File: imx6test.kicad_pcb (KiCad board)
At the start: 2 copper layers, 12 parts

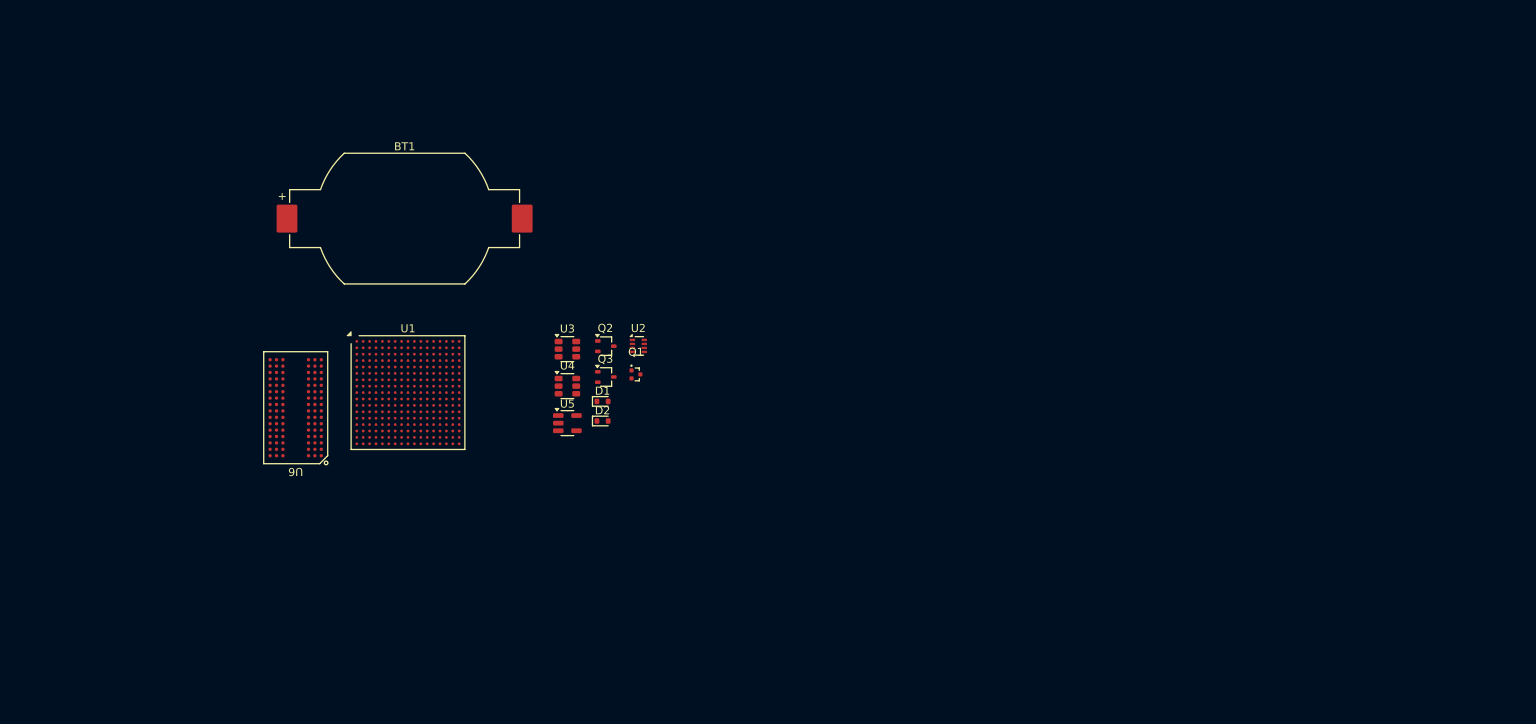
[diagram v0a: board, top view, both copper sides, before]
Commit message: Add in LCSC part numbers for major parts, assign packages
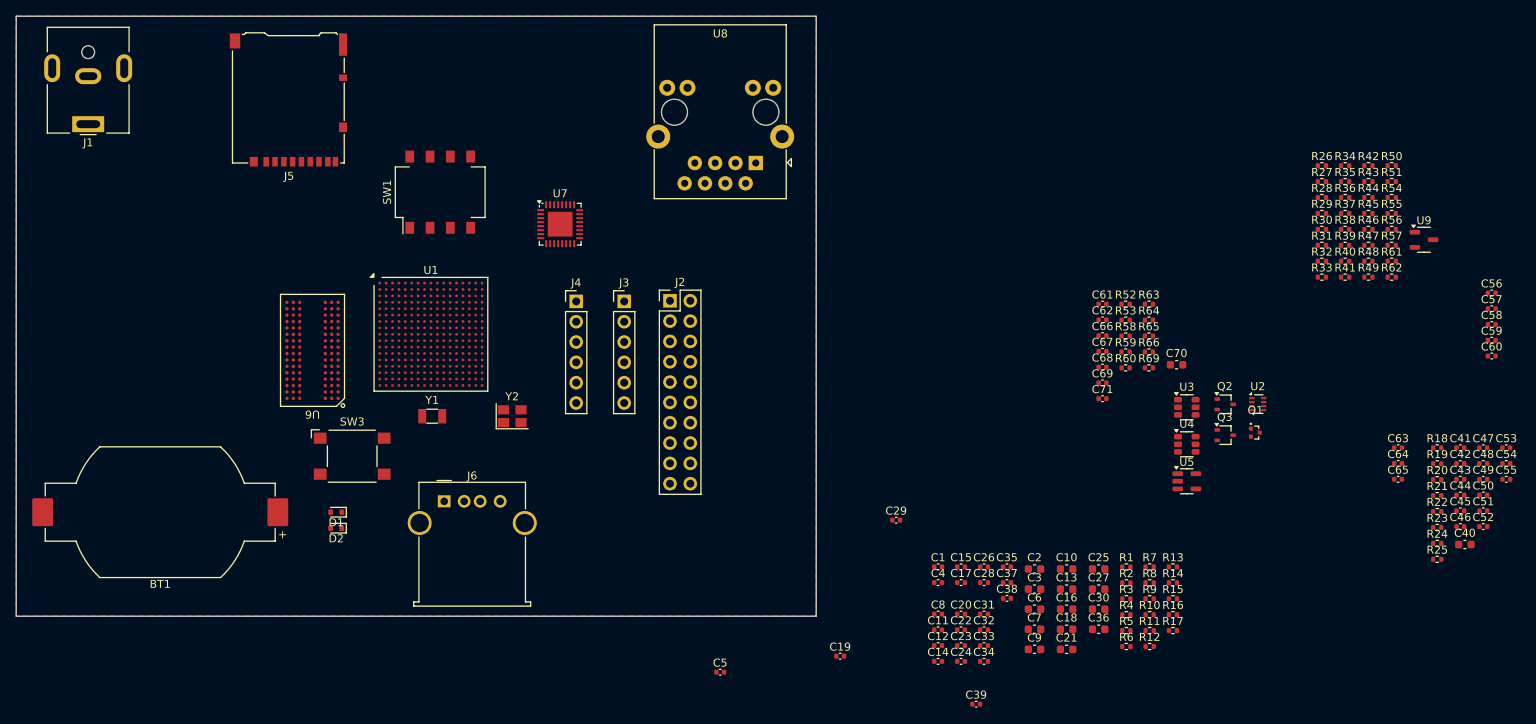
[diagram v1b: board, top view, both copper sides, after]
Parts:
- added C1: 0.1uF, Capacitor_SMD:C_0402_1005Metric, F.Cu at (220.2, 118.8)
- added C10: 10uF, Capacitor_SMD:C_0603_1608Metric, F.Cu at (236.3, 119.1)
- added C11: 0.1uF, Capacitor_SMD:C_0402_1005Metric, F.Cu at (220.2, 126.7)
- added C12: 22pF, Capacitor_SMD:C_0402_1005Metric, F.Cu at (220.2, 128.7)
- added C13: 22uF, Capacitor_SMD:C_0603_1608Metric, F.Cu at (236.3, 121.6)
- added C14: 0.1uF, Capacitor_SMD:C_0402_1005Metric, F.Cu at (220.2, 130.7)
- added C15: 22pF, Capacitor_SMD:C_0402_1005Metric, F.Cu at (223.1, 118.8)
- added C16: 22uF, Capacitor_SMD:C_0603_1608Metric, F.Cu at (236.3, 124.1)
- added C17: 0.1uF, Capacitor_SMD:C_0402_1005Metric, F.Cu at (223.1, 120.8)
- added C18: 22uF, Capacitor_SMD:C_0603_1608Metric, F.Cu at (236.3, 126.6)
- added C19: 0.22uF, Capacitor_SMD:C_0402_1005Metric, F.Cu at (208.0, 130.0)
- added C2: 10uF, Capacitor_SMD:C_0603_1608Metric, F.Cu at (232.3, 119.1)
- added C20: 0.22uF, Capacitor_SMD:C_0402_1005Metric, F.Cu at (223.1, 124.7)
- added C21: 22uF, Capacitor_SMD:C_0603_1608Metric, F.Cu at (236.3, 129.1)
- added C22: 0.22uF, Capacitor_SMD:C_0402_1005Metric, F.Cu at (223.1, 126.7)
- added C23: 0.22uF, Capacitor_SMD:C_0402_1005Metric, F.Cu at (223.1, 128.7)
- added C24: 0.22uF, Capacitor_SMD:C_0402_1005Metric, F.Cu at (223.1, 130.7)
- added C25: 10uF, Capacitor_SMD:C_0603_1608Metric, F.Cu at (240.3, 119.1)
- added C26: 0.22uF, Capacitor_SMD:C_0402_1005Metric, F.Cu at (226.0, 118.8)
- added C27: 10uF, Capacitor_SMD:C_0603_1608Metric, F.Cu at (240.3, 121.6)
- added C28: 0.22uF, Capacitor_SMD:C_0402_1005Metric, F.Cu at (226.0, 120.8)
- added C29: 0.22uF, Capacitor_SMD:C_0402_1005Metric, F.Cu at (215.0, 113.0)
- added C3: 10uF, Capacitor_SMD:C_0603_1608Metric, F.Cu at (232.3, 121.6)
- added C30: 22uF, Capacitor_SMD:C_0603_1608Metric, F.Cu at (240.3, 124.1)
- added C31: 4.7uF, Capacitor_SMD:C_0402_1005Metric, F.Cu at (226.0, 124.7)
- added C32: 0.22uF, Capacitor_SMD:C_0402_1005Metric, F.Cu at (226.0, 126.7)
- added C33: 0.22uF, Capacitor_SMD:C_0402_1005Metric, F.Cu at (226.0, 128.7)
- added C34: 4.7uF, Capacitor_SMD:C_0402_1005Metric, F.Cu at (226.0, 130.7)
- added C35: 0.22uF, Capacitor_SMD:C_0402_1005Metric, F.Cu at (228.8, 118.8)
- added C36: 10uF, Capacitor_SMD:C_0603_1608Metric, F.Cu at (240.3, 126.6)
- added C37: 0.1uF, Capacitor_SMD:C_0402_1005Metric, F.Cu at (228.8, 120.8)
- added C38: 4.7uF, Capacitor_SMD:C_0402_1005Metric, F.Cu at (228.8, 122.8)
- added C39: 0.1uF, Capacitor_SMD:C_0402_1005Metric, F.Cu at (225.0, 136.0)
- added C4: 0.22uF, Capacitor_SMD:C_0402_1005Metric, F.Cu at (220.2, 120.8)
- added C40: 10uF, Capacitor_SMD:C_0603_1608Metric, F.Cu at (286.1, 116.0)
- added C41: 0.22uF, Capacitor_SMD:C_0402_1005Metric, F.Cu at (285.5, 104.0)
- added C42: 0.22uF, Capacitor_SMD:C_0402_1005Metric, F.Cu at (285.5, 105.9)
- added C43: 0.22uF, Capacitor_SMD:C_0402_1005Metric, F.Cu at (285.5, 107.9)
- added C44: 0.22uF, Capacitor_SMD:C_0402_1005Metric, F.Cu at (285.5, 109.9)
- added C45: 0.22uF, Capacitor_SMD:C_0402_1005Metric, F.Cu at (285.5, 111.8)
- added C46: 0.22uF, Capacitor_SMD:C_0402_1005Metric, F.Cu at (285.5, 113.8)
- added C47: 0.22uF, Capacitor_SMD:C_0402_1005Metric, F.Cu at (288.4, 104.0)
- added C48: 0.22uF, Capacitor_SMD:C_0402_1005Metric, F.Cu at (288.4, 105.9)
- added C49: 0.22uF, Capacitor_SMD:C_0402_1005Metric, F.Cu at (288.4, 107.9)
- added C5: 2.2nF, Capacitor_SMD:C_0402_1005Metric, F.Cu at (193.0, 132.0)
- added C50: 0.22uF, Capacitor_SMD:C_0402_1005Metric, F.Cu at (288.4, 109.9)
- added C51: 4.7uF, Capacitor_SMD:C_0402_1005Metric, F.Cu at (288.4, 111.8)
- added C52: 0.1uF, Capacitor_SMD:C_0402_1005Metric, F.Cu at (288.4, 113.8)
- added C53: 0.1uF, Capacitor_SMD:C_0402_1005Metric, F.Cu at (291.3, 104.0)
- added C54: 2.2pF, Capacitor_SMD:C_0402_1005Metric, F.Cu at (291.3, 105.9)
- added C55: 2.2pF, Capacitor_SMD:C_0402_1005Metric, F.Cu at (291.3, 107.9)
- added C56: 18pF, Capacitor_SMD:C_0402_1005Metric, F.Cu at (289.4, 84.6)
- added C57: 18pF, Capacitor_SMD:C_0402_1005Metric, F.Cu at (289.4, 86.6)
- added C58: 18pF, Capacitor_SMD:C_0402_1005Metric, F.Cu at (289.4, 88.5)
- added C59: 18pF, Capacitor_SMD:C_0402_1005Metric, F.Cu at (289.4, 90.5)
- added C6: 10uF, Capacitor_SMD:C_0603_1608Metric, F.Cu at (232.3, 124.1)
- added C60: 0.22uF, Capacitor_SMD:C_0402_1005Metric, F.Cu at (289.4, 92.5)
- added C61: 0.22uF, Capacitor_SMD:C_0402_1005Metric, F.Cu at (240.8, 86.0)
- added C62: 0.22uF, Capacitor_SMD:C_0402_1005Metric, F.Cu at (240.8, 88.0)
- added C63: 0.22uF, Capacitor_SMD:C_0402_1005Metric, F.Cu at (277.7, 104.0)
- added C64: 0.22uF, Capacitor_SMD:C_0402_1005Metric, F.Cu at (277.7, 105.9)
- added C65: 0.22uF, Capacitor_SMD:C_0402_1005Metric, F.Cu at (277.7, 107.9)
- added C66: 0.1uF, Capacitor_SMD:C_0402_1005Metric, F.Cu at (240.8, 89.9)
- added C67: 2.2uF, Capacitor_SMD:C_0402_1005Metric, F.Cu at (240.8, 91.9)
- added C68: 0.1uF, Capacitor_SMD:C_0402_1005Metric, F.Cu at (240.8, 93.9)
- added C69: 0.1uF, Capacitor_SMD:C_0402_1005Metric, F.Cu at (240.8, 95.8)
- added C7: 10uF, Capacitor_SMD:C_0603_1608Metric, F.Cu at (232.3, 126.6)
- added C70: 10uF, Capacitor_SMD:C_0603_1608Metric, F.Cu at (250.1, 93.6)
- added C71: 0.1uF, Capacitor_SMD:C_0402_1005Metric, F.Cu at (240.8, 97.8)
- added C8: 0.1uF, Capacitor_SMD:C_0402_1005Metric, F.Cu at (220.2, 124.7)
- added C9: 10uF, Capacitor_SMD:C_0603_1608Metric, F.Cu at (232.3, 129.1)
- added J1: Barrel_Jack_MountingPin, Connector_BarrelJack:BarrelJack_CUI_PJ-063AH_Horizontal, F.Cu at (114.0, 63.5)
- added J2: Conn_ARM_JTAG_SWD_20, Connector_PinHeader_2.54mm:PinHeader_2x10_P2.54mm_Vertical, F.Cu at (186.7, 85.6)
- added J3: Conn_01x06_Pin, Connector_PinHeader_2.54mm:PinHeader_1x06_P2.54mm_Vertical, F.Cu at (181.0, 85.7)
- added J4: Conn_01x06_Pin, Connector_PinHeader_2.54mm:PinHeader_1x06_P2.54mm_Vertical, F.Cu at (175.0, 85.7)
- added J5: Micro_SD_Card_Det2, Connector_Card:microSD_HC_Hirose_DM3AT-SF-PEJM5, F.Cu at (139.0, 60.5)
- added J6: USB_A, Connector_USB:USB_A_Molex_67643_Horizontal, F.Cu at (158.5, 110.6)
- added R1: 200k 1%, Resistor_SMD:R_0402_1005Metric, F.Cu at (243.8, 118.8)
- added R10: 90.9k, Resistor_SMD:R_0402_1005Metric, F.Cu at (246.7, 124.8)
- added R11: 1k, Resistor_SMD:R_0402_1005Metric, F.Cu at (246.7, 126.8)
- added R12: 953k, Resistor_SMD:R_0402_1005Metric, F.Cu at (246.7, 128.8)
- added R13: 100k, Resistor_SMD:R_0402_1005Metric, F.Cu at (249.6, 118.8)
- added R14: 464k, Resistor_SMD:R_0402_1005Metric, F.Cu at (249.6, 120.8)
- added R15: 200k 1%, Resistor_SMD:R_0402_1005Metric, F.Cu at (249.6, 122.8)
- added R16: 243k, Resistor_SMD:R_0402_1005Metric, F.Cu at (249.6, 124.8)
- added R17: 100k, Resistor_SMD:R_0402_1005Metric, F.Cu at (249.6, 126.8)
- added R18: 10k, Resistor_SMD:R_0402_1005Metric, F.Cu at (282.6, 104.0)
- added R19: 240 1%, Resistor_SMD:R_0402_1005Metric, F.Cu at (282.6, 106.0)
- added R2: 44.2k 1%, Resistor_SMD:R_0402_1005Metric, F.Cu at (243.8, 120.8)
- added R20: 10k, Resistor_SMD:R_0402_1005Metric, F.Cu at (282.6, 107.9)
- added R21: 10k, Resistor_SMD:R_0402_1005Metric, F.Cu at (282.6, 109.9)
- added R22: 240 1%, Resistor_SMD:R_0402_1005Metric, F.Cu at (282.6, 111.9)
- added R23: 1.5k 1%, Resistor_SMD:R_0402_1005Metric, F.Cu at (282.6, 113.9)
- added R24: 1.5k 1%, Resistor_SMD:R_0402_1005Metric, F.Cu at (282.6, 115.9)
- added R25: 470, Resistor_SMD:R_0402_1005Metric, F.Cu at (282.6, 117.9)
- added R26: 10k, Resistor_SMD:R_0402_1005Metric, F.Cu at (268.2, 68.7)
- added R27: 10k, Resistor_SMD:R_0402_1005Metric, F.Cu at (268.2, 70.7)
- added R28: 10k, Resistor_SMD:R_0402_1005Metric, F.Cu at (268.2, 72.7)
- added R29: 10k, Resistor_SMD:R_0402_1005Metric, F.Cu at (268.2, 74.7)
- added R3: 10k, Resistor_SMD:R_0402_1005Metric, F.Cu at (243.8, 122.8)
- added R30: 10k, Resistor_SMD:R_0402_1005Metric, F.Cu at (268.2, 76.7)
- added R31: 10k, Resistor_SMD:R_0402_1005Metric, F.Cu at (268.2, 78.6)
- added R32: 10k, Resistor_SMD:R_0402_1005Metric, F.Cu at (268.2, 80.6)
- added R33: 10k, Resistor_SMD:R_0402_1005Metric, F.Cu at (268.2, 82.6)
- added R34: 10k, Resistor_SMD:R_0402_1005Metric, F.Cu at (271.1, 68.7)
- added R35: 10k, Resistor_SMD:R_0402_1005Metric, F.Cu at (271.1, 70.7)
- added R36: 10k, Resistor_SMD:R_0402_1005Metric, F.Cu at (271.1, 72.7)
- added R37: 10k, Resistor_SMD:R_0402_1005Metric, F.Cu at (271.1, 74.7)
- added R38: 10k, Resistor_SMD:R_0402_1005Metric, F.Cu at (271.1, 76.7)
- added R39: 10k, Resistor_SMD:R_0402_1005Metric, F.Cu at (271.1, 78.6)
- added R4: 10k, Resistor_SMD:R_0402_1005Metric, F.Cu at (243.8, 124.8)
- added R40: 10k, Resistor_SMD:R_0402_1005Metric, F.Cu at (271.1, 80.6)
- added R41: 10k, Resistor_SMD:R_0402_1005Metric, F.Cu at (271.1, 82.6)
- added R42: 10k, Resistor_SMD:R_0402_1005Metric, F.Cu at (274.0, 68.7)
- added R43: 10k, Resistor_SMD:R_0402_1005Metric, F.Cu at (274.0, 70.7)
- added R44: 10k, Resistor_SMD:R_0402_1005Metric, F.Cu at (274.0, 72.7)
- added R45: 10k, Resistor_SMD:R_0402_1005Metric, F.Cu at (274.0, 74.7)
- added R46: 10k, Resistor_SMD:R_0402_1005Metric, F.Cu at (274.0, 76.7)
- added R47: 10k, Resistor_SMD:R_0402_1005Metric, F.Cu at (274.0, 78.6)
- added R48: 10k, Resistor_SMD:R_0402_1005Metric, F.Cu at (274.0, 80.6)
- added R49: 10k, Resistor_SMD:R_0402_1005Metric, F.Cu at (274.0, 82.6)
- added R5: 10k, Resistor_SMD:R_0402_1005Metric, F.Cu at (243.8, 126.8)
- added R50: 1k, Resistor_SMD:R_0402_1005Metric, F.Cu at (276.9, 68.7)
- added R51: 10k, Resistor_SMD:R_0402_1005Metric, F.Cu at (276.9, 70.7)
- added R52: 6.49k, Resistor_SMD:R_0402_1005Metric, F.Cu at (243.7, 86.0)
- added R53: 220, Resistor_SMD:R_0402_1005Metric, F.Cu at (243.7, 88.0)
- added R54: 10k, Resistor_SMD:R_0402_1005Metric, F.Cu at (276.9, 72.7)
- added R55: 1k, Resistor_SMD:R_0402_1005Metric, F.Cu at (276.9, 74.7)
- added R56: 1k, Resistor_SMD:R_0402_1005Metric, F.Cu at (276.9, 76.7)
- added R57: 1k, Resistor_SMD:R_0402_1005Metric, F.Cu at (276.9, 78.6)
- added R58: 220, Resistor_SMD:R_0402_1005Metric, F.Cu at (243.7, 90.0)
- added R59: 1k, Resistor_SMD:R_0402_1005Metric, F.Cu at (243.7, 92.0)
- added R6: 127k, Resistor_SMD:R_0402_1005Metric, F.Cu at (243.8, 128.8)
- added R60: 1k, Resistor_SMD:R_0402_1005Metric, F.Cu at (243.7, 94.0)
- added R61: 10k, Resistor_SMD:R_0402_1005Metric, F.Cu at (276.9, 80.6)
- added R62: 1k, Resistor_SMD:R_0402_1005Metric, F.Cu at (276.9, 82.6)
- added R63: 1k, Resistor_SMD:R_0402_1005Metric, F.Cu at (246.6, 86.0)
- added R64: 1k, Resistor_SMD:R_0402_1005Metric, F.Cu at (246.6, 88.0)
- added R65: 1k, Resistor_SMD:R_0402_1005Metric, F.Cu at (246.6, 90.0)
- added R66: 4.7k, Resistor_SMD:R_0402_1005Metric, F.Cu at (246.6, 92.0)
- added R69: 4.7k, Resistor_SMD:R_0402_1005Metric, F.Cu at (246.6, 94.0)
- added R7: 100k 1%, Resistor_SMD:R_0402_1005Metric, F.Cu at (246.7, 118.8)
- added R8: 133k, Resistor_SMD:R_0402_1005Metric, F.Cu at (246.7, 120.8)
- added R9: 100k 1%, Resistor_SMD:R_0402_1005Metric, F.Cu at (246.7, 122.8)
- added SW1: SW_DIP_x04, Button_Switch_SMD:SW_DIP_SPSTx04_Slide_Omron_A6S-410x_W8.9mm_P2.54mm, F.Cu at (158.0, 72.0)
- added SW3: SW_SPST, Button_Switch_SMD:SW_SPST_Omron_B3FS-100xP, F.Cu at (147.0, 105.0)
- added U7: ~, Package_DFN_QFN:QFN-32-1EP_5x5mm_P0.5mm_EP3.1x3.1mm, F.Cu at (173.0, 76.0)
- added U8: ~, imx6test:HR9011105A, F.Cu at (193.0, 62.0)
- added U9: ~, Package_TO_SOT_SMD:SOT-23-3, F.Cu at (281.0, 77.9)
- added Y1: 32.768k, Crystal:Crystal_SMD_3215-2Pin_3.2x1.5mm, F.Cu at (157.0, 100.0)
- added Y2: 24MHz, Crystal:Crystal_SMD_SeikoEpson_TSX3225-4Pin_3.2x2.5mm, F.Cu at (167.0, 100.0)
- moved Q1 77.8 mm to (259.9, 102.0)
- moved Q2 77.8 mm to (256.1, 98.5)
- moved Q3 77.8 mm to (256.1, 102.4)
- moved U2 77.8 mm to (260.2, 98.5)
- moved U3 77.8 mm to (251.3, 98.9)
- moved U4 77.8 mm to (251.3, 103.5)
- moved U5 77.8 mm to (251.3, 108.1)
- moved BT1 47.8 mm to (123.0, 112.0), turned to 180 degrees
- moved D1 36.1 mm to (145.0, 112.0), turned to 180 degrees
- moved D2 35.9 mm to (145.0, 114.0), turned to 180 degrees
- moved U1 7.83 mm to (156.8, 89.8)
- moved U6 7.47 mm to (142.0, 91.8)
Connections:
- U1 pad A10: unconnected-(U1G-LCD_DATA06-PadA10) -> /Boot and Control/BOOT_CFG1(6)
- U1 pad A11: unconnected-(U1G-LCD_DATA09-PadA11) -> /Boot and Control/BOOT_CFG2(1)
- U1 pad A12: unconnected-(U1G-LCD_DATA14-PadA12) -> /Boot and Control/BOOT_CFG2(6)
- U1 pad A13: unconnected-(U1G-LCD_DATA18-PadA13) -> /Boot and Control/BOOT_CFG3(2)
- U1 pad A14: unconnected-(U1G-LCD_DATA22-PadA14) -> /Boot and Control/BOOT_CFG3(6)
- U1 pad A2: unconnected-(U1I-SD1_DATA3-PadA2) -> Net-(J5-DAT3/CD)
- U1 pad A9: unconnected-(U1G-LCD_DATA01-PadA9) -> /Boot and Control/BOOT_CFG1(1)
- U1 pad B1: unconnected-(U1I-SD1_DATA2-PadB1) -> Net-(J5-DAT2)
- U1 pad B10: unconnected-(U1G-LCD_DATA05-PadB10) -> /Boot and Control/BOOT_CFG1(5)
- U1 pad B11: unconnected-(U1G-LCD_DATA08-PadB11) -> /Boot and Control/BOOT_CFG2(0)
- U1 pad B12: unconnected-(U1G-LCD_DATA13-PadB12) -> /Boot and Control/BOOT_CFG2(5)
- U1 pad B13: unconnected-(U1G-LCD_DATA17-PadB13) -> /Boot and Control/BOOT_CFG3(1)
- U1 pad B14: unconnected-(U1G-LCD_DATA21-PadB14) -> /Boot and Control/BOOT_CFG3(5)
- U1 pad B16: unconnected-(U1G-LCD_DATA23-PadB16) -> /Boot and Control/BOOT_CFG3(7)
- U1 pad B2: unconnected-(U1I-SD1_DATA1-PadB2) -> Net-(J5-DAT1)
- U1 pad B3: unconnected-(U1I-SD1_DATA0-PadB3) -> Net-(J5-DAT0)
- U1 pad B9: unconnected-(U1G-LCD_DATA00-PadB9) -> /Boot and Control/BOOT_CFG1(0)
- U1 pad C1: unconnected-(U1I-SD1_CLK-PadC1) -> Net-(J5-CLK)
- U1 pad C10: unconnected-(U1G-LCD_DATA04-PadC10) -> /Boot and Control/BOOT_CFG1(4)
- U1 pad C12: unconnected-(U1G-LCD_DATA12-PadC12) -> /Boot and Control/BOOT_CFG2(4)
- U1 pad C13: unconnected-(U1G-LCD_DATA16-PadC13) -> /Boot and Control/BOOT_CFG3(0)
- U1 pad C14: unconnected-(U1G-LCD_DATA20-PadC14) -> /Boot and Control/BOOT_CFG3(4)
- U1 pad C2: unconnected-(U1I-SD1_CMD-PadC2) -> Net-(J5-CMD)
- U1 pad C4: unconnected-(U1I-NVCC_SD1-PadC4) -> +3.3V
- U1 pad D10: unconnected-(U1G-LCD_DATA03-PadD10) -> /Boot and Control/BOOT_CFG1(3)
- U1 pad D11: unconnected-(U1G-LCD_DATA07-PadD11) -> /Boot and Control/BOOT_CFG1(7)
- U1 pad D12: unconnected-(U1G-LCD_DATA11-PadD12) -> /Boot and Control/BOOT_CFG2(3)
- U1 pad D13: unconnected-(U1G-LCD_DATA15-PadD13) -> /Boot and Control/BOOT_CFG2(7)
- U1 pad D14: unconnected-(U1G-LCD_DATA19-PadD14) -> /Boot and Control/BOOT_CFG3(3)
- U1 pad D15: unconnected-(U1F-ENET1_RX_ER-PadD15) -> Net-(U1F-ENET1_RX_ER)
- U1 pad E10: unconnected-(U1G-LCD_DATA02-PadE10) -> /Boot and Control/BOOT_CFG1(2)
- U1 pad E12: unconnected-(U1G-LCD_DATA10-PadE12) -> /Boot and Control/BOOT_CFG2(2)
- U1 pad E13: unconnected-(U1G-NVCC_LCD-PadE13) -> +3.3V
- U1 pad E14: unconnected-(U1F-ENET1_TX_DATA1-PadE14) -> Net-(U1F-ENET1_TX_DATA1)
- U1 pad E15: unconnected-(U1F-ENET1_TX_DATA0-PadE15) -> Net-(U1F-ENET1_TX_DATA0)
- U1 pad E16: unconnected-(U1F-ENET1_RX_EN-PadE16) -> ENET_CONFIG2
- U1 pad E17: unconnected-(U1F-ENET1_RX_DATA1-PadE17) -> PHYAD2
- U1 pad E7: unconnected-(U1C-NVCC_NAND-PadE7) -> +3.3V
- U1 pad F13: unconnected-(U1F-NVCC_ENET-PadF13) -> +3.3V
- U1 pad F14: unconnected-(U1F-ENET1_TX_CLK-PadF14) -> ENET_TX_CLK
- U1 pad F15: unconnected-(U1F-ENET1_TX_EN-PadF15) -> Net-(U1F-ENET1_TX_EN)
- U1 pad F16: unconnected-(U1F-ENET1_RX_DATA0-PadF16) -> ENET_DUPLEX
- U1 pad F4: unconnected-(U1D-NVCC_CSI-PadF4) -> +3.3V
- U1 pad H13: unconnected-(U1K-NVCC_UART-PadH13) -> +3.3V
- U1 pad H14: unconnected-(U1K-~{UART2_RTS}-PadH14) -> Net-(J4-Pin_6)
- U1 pad J13: unconnected-(U1E-NVCC_GPIO-PadJ13) -> +3.3V
- U1 pad J14: unconnected-(U1K-~{UART1_RTS}-PadJ14) -> Net-(J3-Pin_6)
- U1 pad J15: unconnected-(U1K-~{UART2_CTS}-PadJ15) -> Net-(J4-Pin_2)
- U1 pad J16: unconnected-(U1K-UART2_RX_DATA-PadJ16) -> Net-(J4-Pin_4)
- U1 pad J17: unconnected-(U1K-UART2_TX_DATA-PadJ17) -> Net-(J4-Pin_5)
- U1 pad K13: unconnected-(U1E-GPIO1_IO00-PadK13) -> GND
- U1 pad K14: unconnected-(U1K-UART1_TX_DATA-PadK14) -> Net-(J3-Pin_5)
- U1 pad K15: unconnected-(U1K-~{UART1_CTS}-PadK15) -> Net-(J3-Pin_2)
- U1 pad K16: unconnected-(U1K-UART1_RX_DATA-PadK16) -> Net-(J3-Pin_4)
- U1 pad K17: unconnected-(U1E-GPIO1_IO06-PadK17) -> ENET_MDIO
- U1 pad L13: unconnected-(U1J-VDDA_ADC_3P3-PadL13) -> +3.3V
- U1 pad L16: unconnected-(U1E-GPIO1_IO07-PadL16) -> ENE_MDC
- U1 pad M13: unconnected-(U1J-ADC_VREFH-PadM13) -> +3.3V
- U1 pad M14: unconnected-(U1K-JTAG_TCK-PadM14) -> Net-(J2-TCK/SWCLK)
- U1 pad M17: unconnected-(U1E-GPIO1_IO05-PadM17) -> SD1_VSELECT
- U1 pad N14: unconnected-(U1K-~{JTAG_TRST}-PadN14) -> Net-(J2-~{TRST})
- U1 pad N15: unconnected-(U1K-JTAG_TDO-PadN15) -> Net-(J2-TDO/SWO)
- U1 pad N16: unconnected-(U1K-JTAG_TDI-PadN16) -> Net-(J2-TDI)
- U1 pad N8: unconnected-(U1K-SNVS_TAMPER5-PadN8) -> ENET_~{INT}
- U1 pad P10: unconnected-(U1K-SNVS_TAMPER3-PadP10) -> GPIO_DVFS
- U1 pad P14: unconnected-(U1K-JTAG_TMS-PadP14) -> Net-(J2-TMS/SWDIO)
- U1 pad P15: unconnected-(U1K-JTAG_MOD-PadP15) -> Net-(U1K-JTAG_MOD)
- U1 pad P8: unconnected-(U1K-~{POR}-PadP8) -> Net-(U1K-~{POR})
- U1 pad R12: unconnected-(U1H-VDD_USB_CAP-PadR12) -> Net-(U1H-VDD_USB_CAP)
- U1 pad R8: unconnected-(U1K-ONOFF-PadR8) -> Net-(SW3-A)
- U1 pad T10: unconnected-(U1K-BOOT_MODE0-PadT10) -> Net-(U1K-BOOT_MODE0)
- U1 pad T11: unconnected-(U1K-RTC_XTALI-PadT11) -> Net-(U1K-RTC_XTALI)
- U1 pad T15: unconnected-(U1H-USB_OTG1_DN-PadT15) -> Net-(J6-D-)
- U1 pad T16: unconnected-(U1K-XTALI-PadT16) -> Net-(U1K-XTALI)
- U1 pad T17: unconnected-(U1K-XTALO-PadT17) -> Net-(U1K-XTALO)
- U1 pad T9: unconnected-(U1K-SNVS_PMIC_ON_REQ-PadT9) -> PMIC_ON_REQ
- U1 pad U10: unconnected-(U1K-BOOT_MODE1-PadU10) -> Net-(U1K-BOOT_MODE1)
- U1 pad U11: unconnected-(U1K-RTC_XTALO-PadU11) -> Net-(U1K-RTC_XTALO)
- U1 pad U15: unconnected-(U1H-USB_OTG1_DP-PadU15) -> Net-(J6-D+)
- U1 pad U9: unconnected-(U1K-CCM_PMIC_STBY_REQ-PadU9) -> PMIC_STBY_REQ
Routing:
- added copper zone on F.Cu, net GND
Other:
- board outline added: 100 x 75 mm
- copper layers 2 -> 4
